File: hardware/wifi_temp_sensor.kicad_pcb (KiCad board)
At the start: 2 copper layers, 50 x 77 mm, 46 parts, among them IC2 BQ21040DBVR, J2 Batt_Conn, J3 Conn_02x03_Odd_Even, P1 USB_C_Plug_USB2.0, Q1 SSM6L09FUTE85LF, Q2 AO3401A, Q3 BSS214NW, SW1 SW_SPST, SW2 SW_Push, U1 ESP32-C3-WROOM-02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

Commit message: Sorting out BOM
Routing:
- net GND: track 75.2 -> 70.7 mm
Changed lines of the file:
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@@
   (via (at 194.945 97.155) (size 0.8) (drill 0.4) (layers "F.Cu" "B.Cu") (net 1))
   (via (at 206.395 91.44) (size 0.8) (drill 0.4) (layers "F.Cu" "B.Cu") (free) (net 1))
-  (segment (start 226.63 40.07) (end 226.06 40.64) (width 0.5) (layer "B.Cu") (net 1))
-  (segment (start 226.63 36.39) (end 226.63 40.07) (width 0.5) (layer "B.Cu") (net 1))
   (segment (start 184.245 93.892501) (end 184.245 101.06) (width 1) (layer "F.Cu") (net 2))
   (segment (start 185.42 91.12) (end 185.105 90.805) (width 0.5) (layer "F.Cu") (net 2))
@@
       )
     )
+  )
+  (zone (net 1) (net_name "GND") (layer "B.Cu") (hatch edge 0.5)
+    (priority 2)
+    (connect_pads (clearance 0.5))
+    (min_thickness 0.25) (filled_areas_thickness no)
+    (fill yes (thermal_gap 0.5) (thermal_bridge_width 0.5))
+    (polygon
+      (pts
+        (xy 228.6 38.735)
+        (xy 228.5 34.25)
+        (xy 217.75 34.25)
+        (xy 217.5 38.75)
+      )
+    )

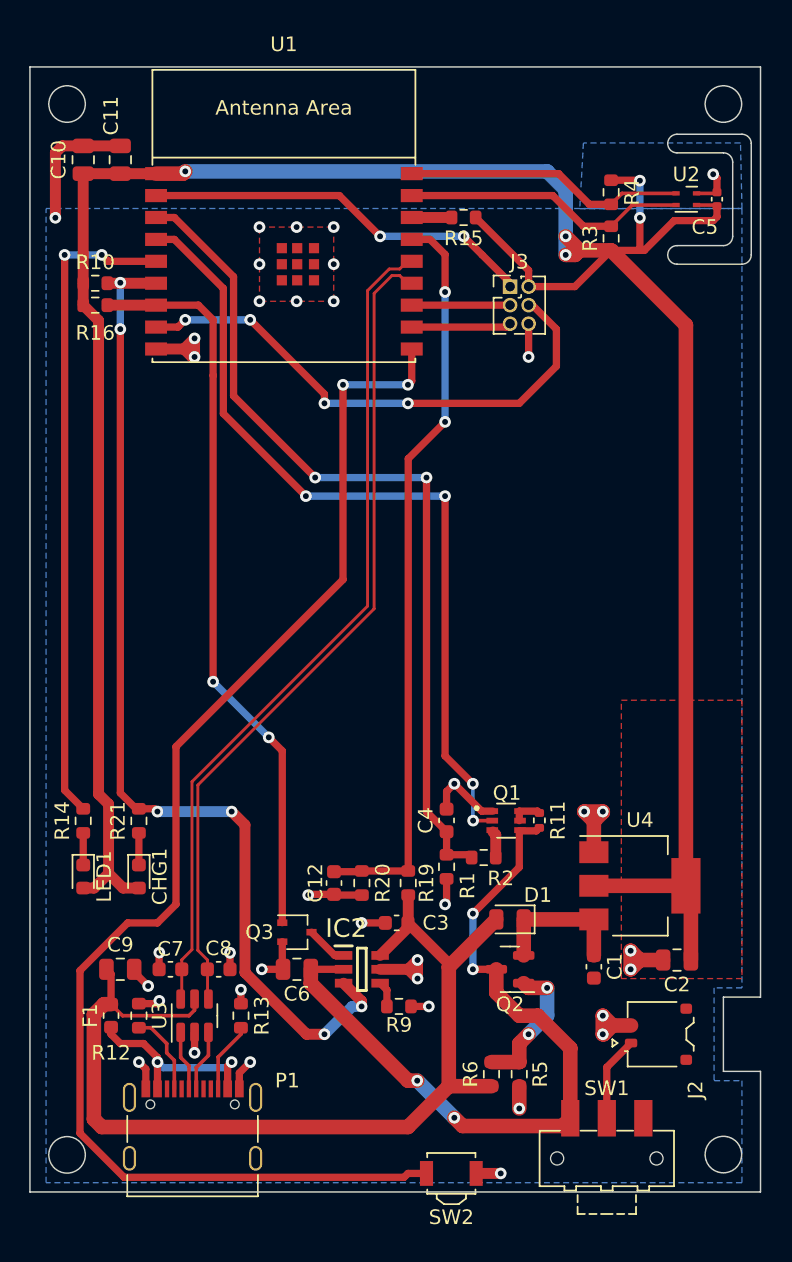
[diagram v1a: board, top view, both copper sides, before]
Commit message: re-routed util switch to GPIO4 for deep sleep wakeup, re-routed USB to get the differental impedance to nearer to 90ohms
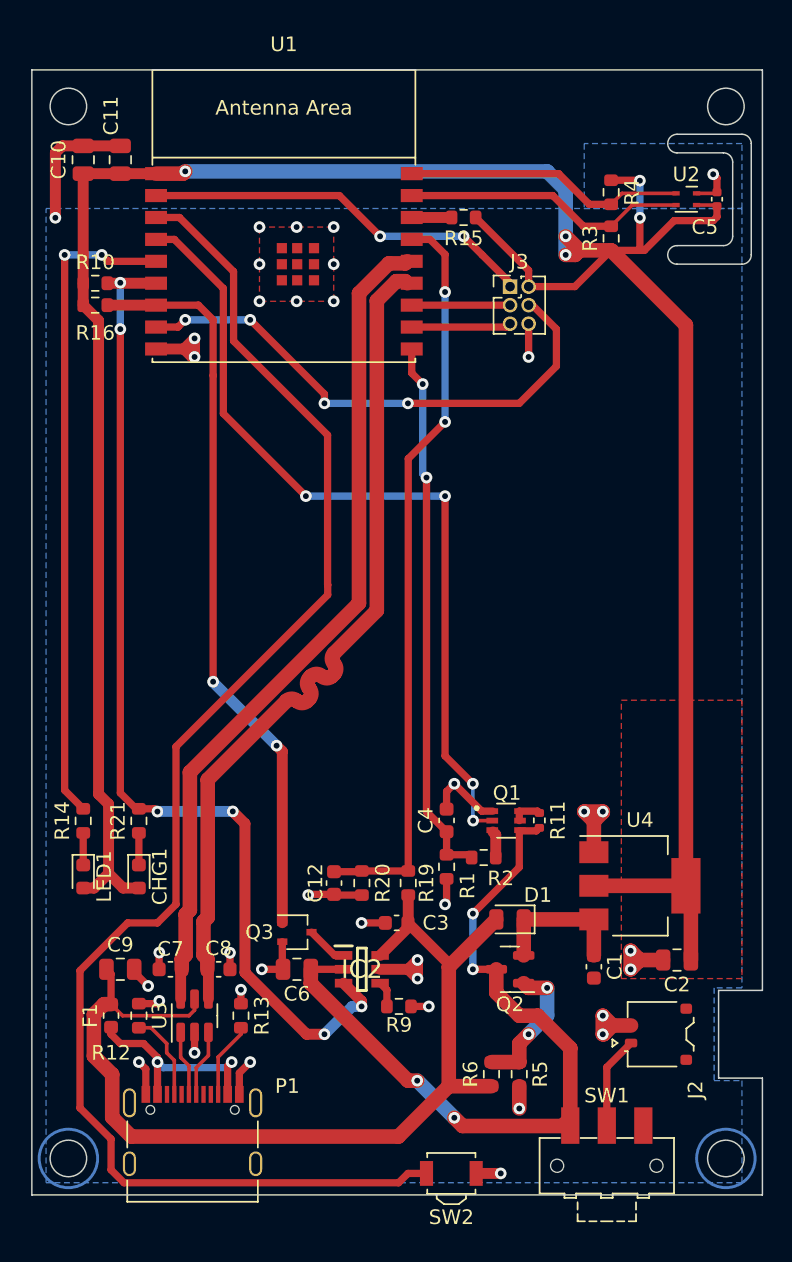
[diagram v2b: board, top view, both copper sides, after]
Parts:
- R1, R11, R2: value 100K -> 100k
- R12, R13: value 5.1K -> 5.1k
- R19: value 33K -> 33k
- R20, R5: value 10K -> 10k
- R6: value 1K -> 1k
- moved SW1 0.50 mm to (219.3, 104.2)
- moved P1 0.38 mm to (191.0, 101.9)
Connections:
- U1 pad 10: UTIL -> V_BAT_MEAS
- U1 pad 3: V_BAT_MEAS -> UTIL
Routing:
- net V_BAT_MEAS: track 58.8 -> 37.4 mm
- net UTIL: track 92.0 -> 102.3 mm, vias 2 -> 0
- net D-: track 56.9 -> 58.0 mm
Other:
- outline, holes or cut-outs redrawn

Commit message: Fixed up errors, ready for review
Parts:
- added R7: 10k, Resistor_SMD:R_0603_1608Metric, F.Cu at (201.0, 87.0)
- moved C12 1.34 mm to (200.8, 83.6)
- moved R20 1.34 mm to (202.8, 83.6)
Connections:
- Q3 pad 1: CHG_ENABLE -> ~{CHG_ENABLE}
- R16 pad 2: CHG_ENABLE -> VBAT_MEAS_EN
- U1 pad 4: VBAT_MEAS_EN -> ~{CHG_ENABLE}
- U1 pad 7: CHG_ENABLE -> VBAT_MEAS_EN
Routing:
- net ~{CHG_ENABLE}: track 0.00 -> 57.0 mm, vias 0 -> 2
- net CHG_ENABLE: track 50.9 -> 0.00 mm, vias 2 -> 0
- net V_USB: track 68.5 -> 72.4 mm
- net Net-(IC2-TS): track 2.85 -> 6.40 mm
- net GND: track 70.7 -> 73.5 mm

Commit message: minor changes
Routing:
- added copper zone on B.Cu, net unconnected-(P1-SHIELD-PadS1)
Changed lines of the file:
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@@
     (property "ki_description" "0.8A Single Input Single-Cell Li-Ion and Li-Pol Battery Charger")
     (attr smd)
-    (fp_text reference "IC2" (at 0 0) (layer "F.SilkS")
+    (fp_text reference "IC2" (at -0.335 4.195 180) (layer "F.SilkS")
         (effects (font (size 1.27 1.27) (thickness 0.254)))
     )
@@
     (property "ki_keywords" "R resistor")
     (attr smd)
-    (fp_text reference "R7" (at 2.25 0) (layer "F.SilkS")
+    (fp_text reference "R7" (at 0.75 1.75) (layer "F.SilkS")
         (effects (font (size 1 1) (thickness 0.15)))
     )
@@
         (xy 228.6 38.735)
         (xy 228.6 34.29)
-        (xy 217.805 34.29)
-        (xy 217.805 38.735)
+        (xy 217.555 34.29)
+        (xy 217.555 38.735)
       )
     )
@@
       )
     )
+  )
+  (zone (net 22) (net_name "unconnected-(P1-SHIELD-PadS1)") (layer "B.Cu") (hatch edge 0.5)
+    (priority 4)
+    (connect_pads (clearance 0.5))
+    (min_thickness 0.25) (filled_areas_thickness no)
+    (fill yes (thermal_gap 0.5) (thermal_bridge_width 0.5))
+    (polygon
+      (pts
+        (xy 185 98.25)
+        (xy 197 98.25)
+        (xy 197 105.5)
+        (xy 185 105.5)
+      )
+    )
